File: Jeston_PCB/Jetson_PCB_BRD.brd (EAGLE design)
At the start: 87 x 50 mm, 4 parts, among them Q2 NTD3055L104G

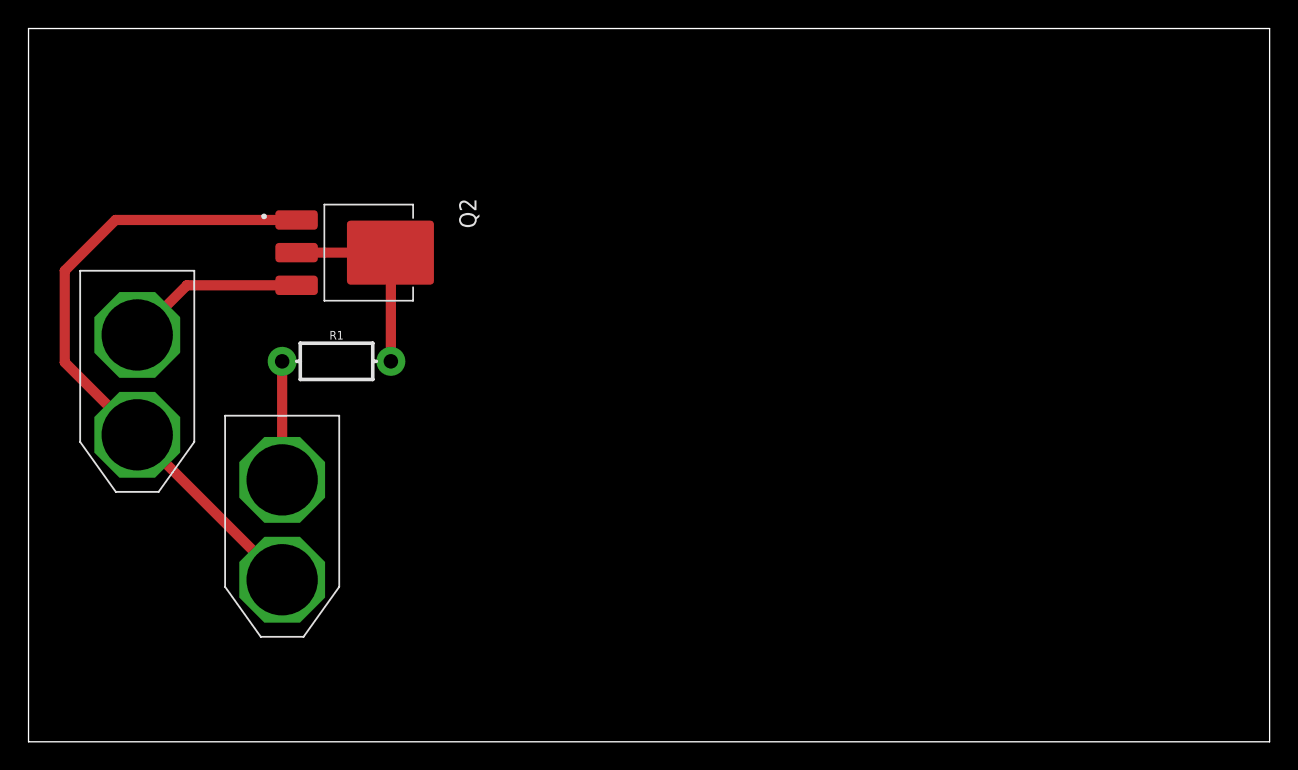
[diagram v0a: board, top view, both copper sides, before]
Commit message: replacing ports to pins, different resistor footprint
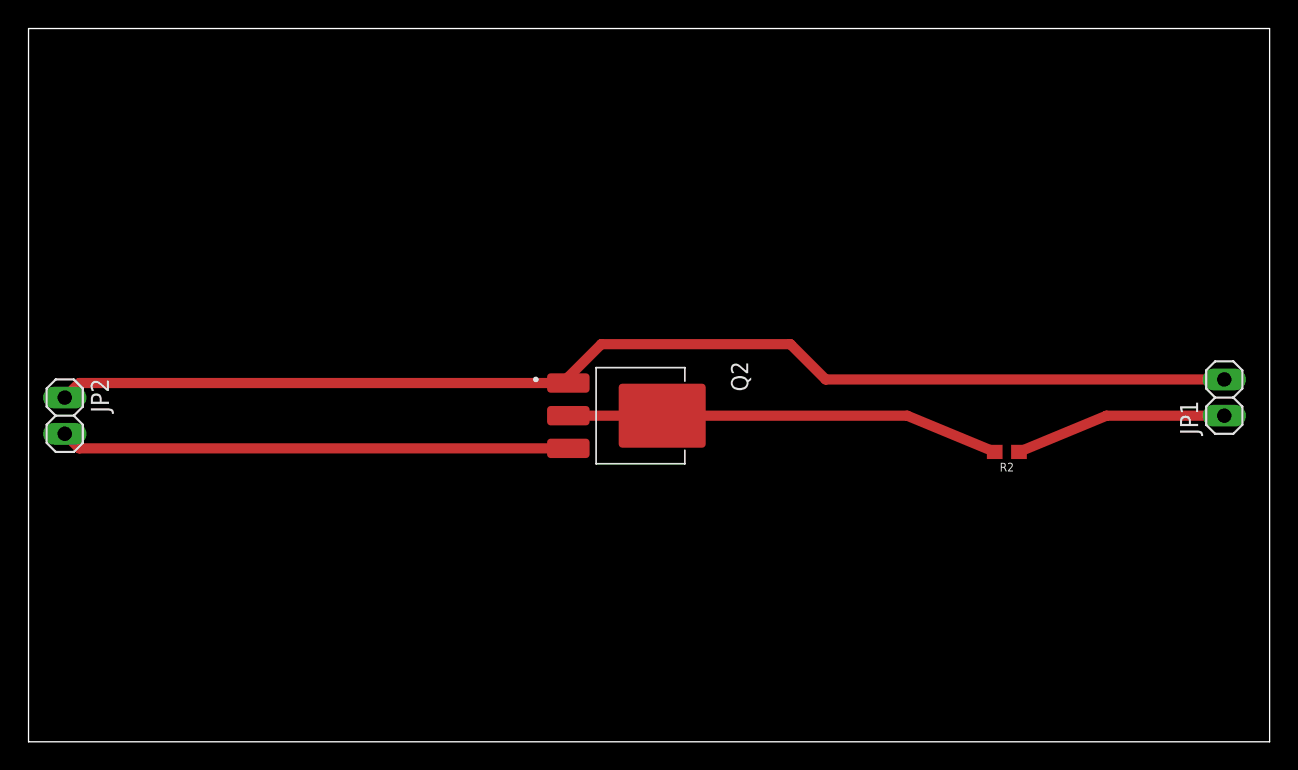
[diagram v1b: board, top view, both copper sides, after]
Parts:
- removed R1: (no value), SparkFun-Resistors:AXIAL-0.3-KIT
- removed U$1, U$2: XT60, XT60:XT60
- added JP1, JP2: (no value), pinhead:1X02
- added R2: 1.8M, SparkFun-Resistors:0603
- moved Q2 22.2 mm to (41.9, 22.9)
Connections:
- net N$1: now also JP1.2, JP2.1; no longer U$1.-, U$2.-
- net N$2: now also JP1.1, R2.1; no longer R1.P$1, U$2.+
- net N$3: now also R2.2; no longer R1.P$2
- net N$4: now also JP2.2; no longer U$1.+
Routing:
- net N$1: track 45.7 -> 84.1 mm
- net N$4: track 12.6 -> 35.7 mm
- net N$3: track 14.2 -> 30.4 mm
- net N$2: track 8.31 -> 14.9 mm
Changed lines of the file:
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@@
 <layer number="43" name="vRestrict" color="2" fill="10" visible="yes" active="yes"/>
 <layer number="44" name="Drills" color="7" fill="1" visible="no" active="yes"/>
-<layer number="45" name="Holes" color="7" fill="1" visible="yes" active="yes"/>
+<layer number="45" name="Holes" color="7" fill="1" visible="no" active="yes"/>
 <layer number="46" name="Milling" color="3" fill="1" visible="no" active="yes"/>
 <layer number="47" name="Measures" color="7" fill="1" visible="no" active="yes"/>
@@
 </autorouter>
 <elements>
-<element name="Q2" library="Transistor" library_urn="urn:adsk.eagle:library:11396518" package="DPAK4" package3d_urn="urn:adsk.eagle:package:10893256/2" value="NTD3055L104G" x="22.86" y="34.29" smashed="yes" rot="R270">
-<attribute name="CREATED_BY" value="PCBLayout.com" x="12.7" y="11.43" size="1.778" layer="27" rot="R270" display="off"/>
-<attribute name="MANUFACTURER" value="ON SEMICONDUCTORS" x="12.7" y="11.43" size="1.778" layer="27" rot="R270" display="off"/>
-<attribute name="MPN" value="NTD3055L104G" x="12.7" y="11.43" size="1.778" layer="27" rot="R270" display="off"/>
-<attribute name="NAME" x="30.1975" y="38.1" size="1.2" layer="25" ratio="10" rot="R270"/>
-<attribute name="PACKAGE" value="DPAK-4" x="12.7" y="11.43" size="1.778" layer="27" rot="R270" display="off"/>
-<attribute name="VALUE" x="13.97" y="38.1" size="1.2" layer="27" ratio="10" rot="R270"/>
+<element name="JP1" library="pinhead" library_urn="urn:adsk.eagle:library:325" package="1X02" package3d_urn="urn:adsk.eagle:package:22435/2" value="" x="83.82" y="24.13" smashed="yes" rot="R90">
+<attribute name="NAME" x="81.9912" y="21.5138" size="1.27" layer="25" ratio="10" rot="R90"/>
+<attribute name="POPULARITY" value="98" x="105.41" y="40.64" size="1.778" layer="27" rot="R90" display="off"/>
+<attribute name="VALUE" x="86.995" y="21.59" size="1.27" layer="27" rot="R90"/>
 </element>
-<element name="R1" library="SparkFun-Resistors" package="AXIAL-0.3-KIT" value=" " x="21.59" y="26.67" smashed="yes">
-<attribute name="NAME" x="21.59" y="28.194" size="0.6096" layer="25" font="vector" ratio="20" align="bottom-center"/>
-<attribute name="PROD_ID" value=" " x="39.37" y="-10.16" size="1.778" layer="27" display="off"/>
-<attribute name="VALUE" x="22.86" y="25.146" size="0.6096" layer="27" font="vector" ratio="20" align="top-center"/>
+<element name="JP2" library="pinhead" library_urn="urn:adsk.eagle:library:325" package="1X02" package3d_urn="urn:adsk.eagle:package:22435/2" value="" x="2.54" y="22.86" smashed="yes" rot="R270">
+<attribute name="NAME" x="4.3688" y="25.4762" size="1.27" layer="25" ratio="10" rot="R270"/>
+<attribute name="POPULARITY" value="98" x="-19.05" y="0" size="1.778" layer="27" rot="R270" display="off"/>
+<attribute name="VALUE" x="-0.635" y="25.4" size="1.27" layer="27" rot="R270"/>
 </element>
-<element name="U$1" library="XT60" package="XT60" value="XT60" x="7.62" y="33.02" smashed="yes" rot="R270"/>
-<element name="U$2" library="XT60" package="XT60" value="XT60" x="17.78" y="22.86" smashed="yes" rot="R270"/>
+<element name="Q2" library="Transistor" library_urn="urn:adsk.eagle:library:11396518" package="DPAK4" package3d_urn="urn:adsk.eagle:package:10893256/2" value="NTD3055L104G" x="41.91" y="22.86" smashed="yes" rot="R270">
+<attribute name="CREATED_BY" value="PCBLayout.com" x="31.75" y="0" size="1.778" layer="27" rot="R270" display="off"/>
+<attribute name="MANUFACTURER" value="ON SEMICONDUCTORS" x="31.75" y="0" size="1.778" layer="27" rot="R270" display="off"/>
+<attribute name="MPN" value="NTD3055L104G" x="31.75" y="0" size="1.778" layer="27" rot="R270" display="off"/>
+<attribute name="NAME" x="49.2475" y="26.67" size="1.2" layer="25" ratio="10" rot="R270"/>
+<attribute name="PACKAGE" value="DPAK-4" x="31.75" y="0" size="1.778" layer="27" rot="R270" display="off"/>
+<attribute name="VALUE" x="33.02" y="26.67" size="1.2" layer="27" ratio="10" rot="R270"/>
+</element>
+<element name="R2" library="SparkFun-Resistors" package="0603" value="1.8M" x="68.58" y="20.32" smashed="yes" rot="R180">
+<attribute name="NAME" x="68.58" y="19.558" size="0.6096" layer="25" font="vector" ratio="20" rot="R180" align="bottom-center"/>
+<attribute name="PROD_ID" value="RES-13994" x="68.58" y="20.32" size="1.778" layer="27" rot="R180" display="off"/>
+<attribute name="VALUE" x="68.58" y="21.082" size="0.6096" layer="27" font="vector" ratio="20" rot="R180" align="top-center"/>
+</element>
 </elements>
 <signals>
 <signal name="N$1">
 <contactref element="Q2" pad="1"/>
-<contactref element="U$1" pad="-"/>
-<wire x1="18.79" y1="36.58" x2="6.1" y2="36.58" width="0.71628125" layer="1"/>
-<wire x1="2.54" y1="33.02" x2="6.1" y2="36.58" width="0.71628125" layer="1"/>
-<wire x1="2.54" y1="33.02" x2="2.54" y2="26.6" width="0.71628125" layer="1"/>
-<wire x1="2.54" y1="26.6" x2="7.585" y2="21.555" width="0.71628125" layer="1"/>
-<wire x1="7.585" y1="21.555" x2="7.62" y2="21.52" width="0.1524" layer="1"/>
-<wire x1="17.78" y1="11.36" x2="7.62" y2="21.52" width="0.71628125" layer="1"/>
-<contactref element="U$2" pad="-"/>
+<contactref element="JP2" pad="1"/>
+<contactref element="JP1" pad="2"/>
+<wire x1="37.84" y1="25.15" x2="3.56" y2="25.15" width="0.71628125" layer="1"/>
+<wire x1="2.54" y1="24.13" x2="3.56" y2="25.15" width="0.71628125" layer="1"/>
+<wire x1="40.14996875" y1="27.8736" x2="37.84" y2="25.56363125" width="0.71628125" layer="1"/>
+<wire x1="37.84" y1="25.15" x2="37.84" y2="25.56363125" width="0.71628125" layer="1"/>
+<wire x1="40.14996875" y1="27.8736" x2="53.4064" y2="27.8736" width="0.71628125" layer="1"/>
+<wire x1="55.88" y1="25.4" x2="83.82" y2="25.4" width="0.71628125" layer="1"/>
+<wire x1="55.88" y1="25.4" x2="53.4064" y2="27.8736" width="0.71628125" layer="1"/>
 </signal>
 <signal name="N$2">
-<contactref element="R1" pad="P$1"/>
-<contactref element="U$2" pad="+"/>
-<wire x1="17.78" y1="26.67" x2="17.78" y2="18.36" width="0.71628125" layer="1"/>
+<contactref element="JP1" pad="1"/>
+<wire x1="83.82" y1="22.86" x2="75.5621" y2="22.86" width="0.71628125" layer="1"/>
+<wire x1="75.5621" y1="22.86" x2="69.43" y2="20.32" width="0.71628125" layer="1"/>
+<contactref element="R2" pad="1"/>
 </signal>
 <signal name="N$3">
-<contactref element="R1" pad="P$2"/>
 <contactref element="Q2" pad="2"/>
 <contactref element="Q2" pad="4"/>
-<wire x1="25.37" y1="34.29" x2="18.79" y2="34.29" width="0.71628125" layer="1"/>
-<wire x1="25.4" y1="26.67" x2="25.4" y2="34.26" width="0.71628125" layer="1"/>
-<wire x1="25.4" y1="34.26" x2="25.37" y2="34.29" width="0.71628125" layer="1"/>
+<wire x1="37.84" y1="22.86" x2="44.42" y2="22.86" width="0.71628125" layer="1"/>
+<contactref element="R2" pad="2"/>
+<wire x1="44.42" y1="22.86" x2="61.5979" y2="22.86" width="0.71628125" layer="1"/>
+<wire x1="61.5979" y1="22.86" x2="67.73" y2="20.32" width="0.71628125" layer="1"/>
 </signal>
 <signal name="N$4">
 <contactref element="Q2" pad="3"/>
-<contactref element="U$1" pad="+"/>
-<wire x1="18.79" y1="32" x2="11.1" y2="32" width="0.71628125" layer="1"/>
-<wire x1="7.62" y1="28.52" x2="11.1" y2="32" width="0.71628125" layer="1"/>
+<contactref element="JP2" pad="2"/>
+<wire x1="37.84" y1="20.57" x2="3.56" y2="20.57" width="0.71628125" layer="1"/>
+<wire x1="2.54" y1="21.59" x2="3.56" y2="20.57" width="0.71628125" layer="1"/>
 </signal>
 </signals>
